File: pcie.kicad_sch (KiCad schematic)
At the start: 10 parts, among them U1 MPFS250T-FCVG484, U17 DSC557-0343FI1

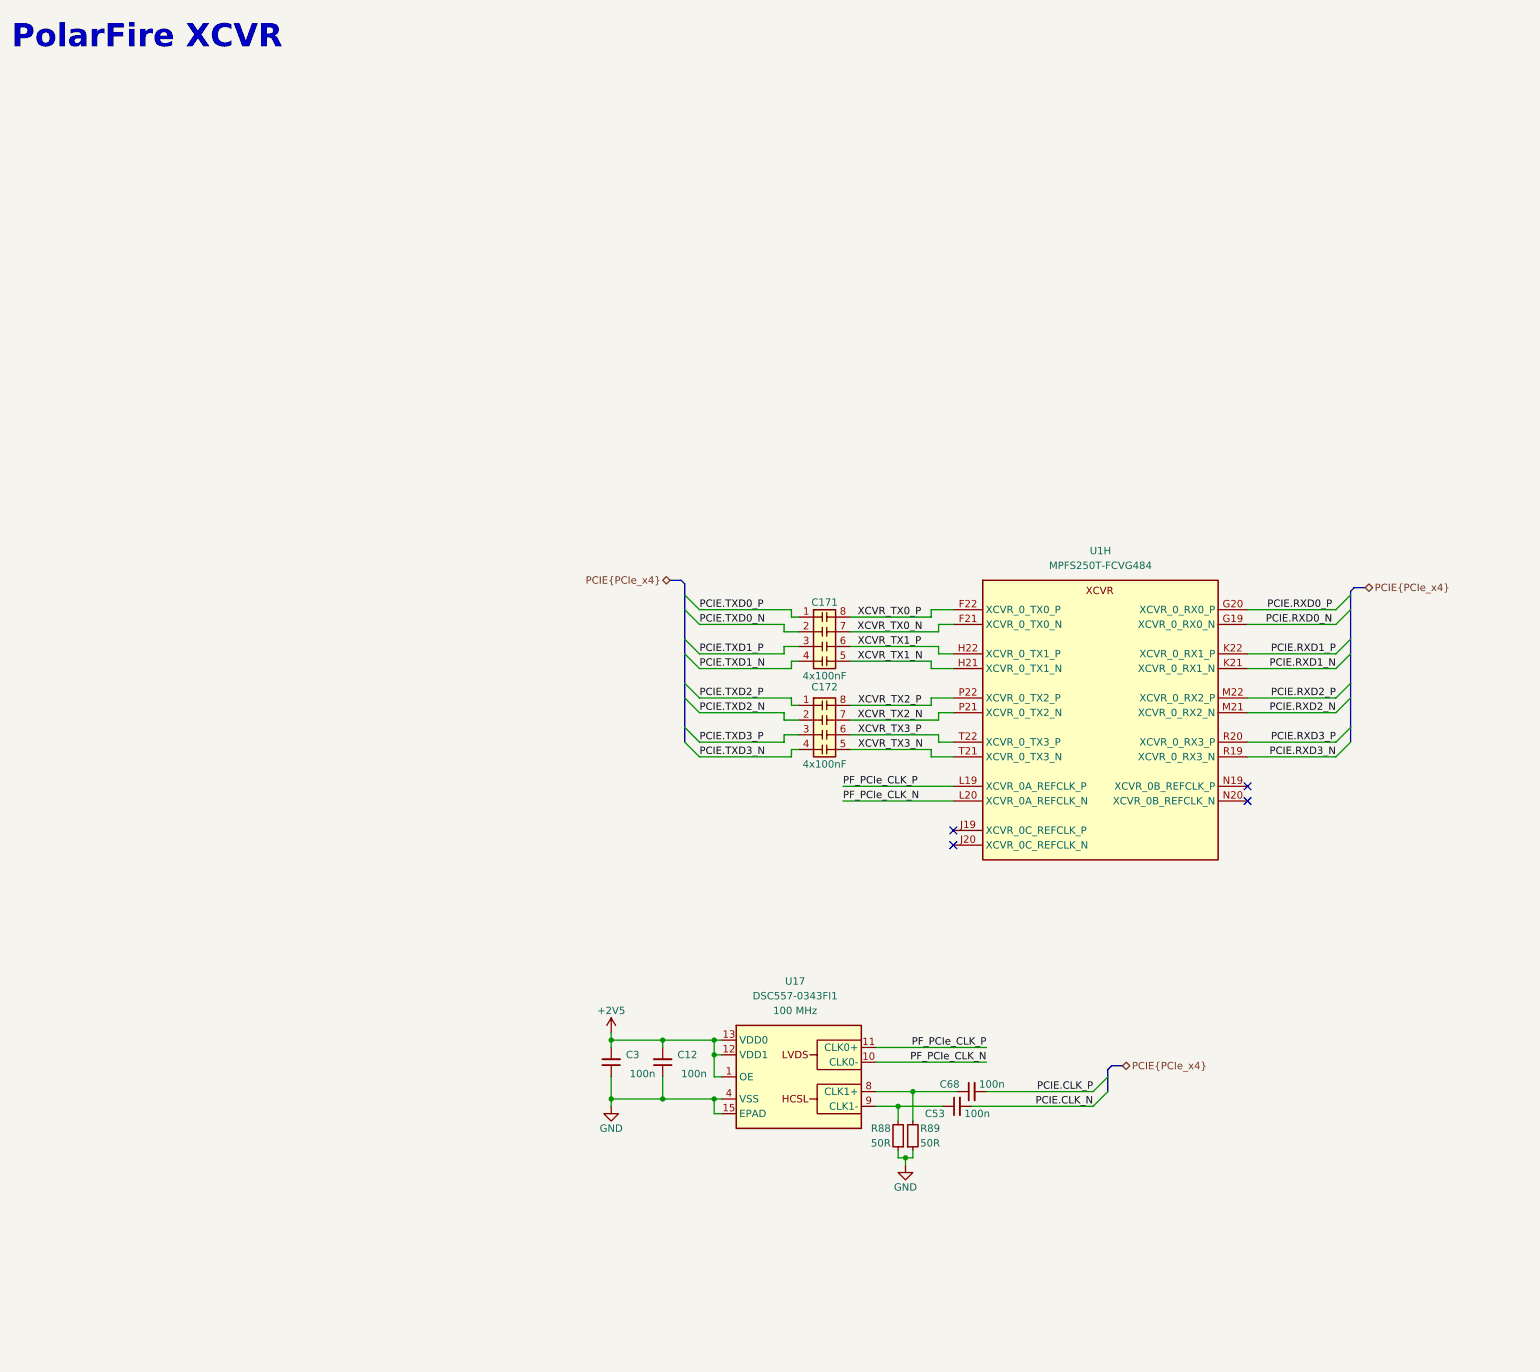
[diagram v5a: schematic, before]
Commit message: [#57422] Align schematics
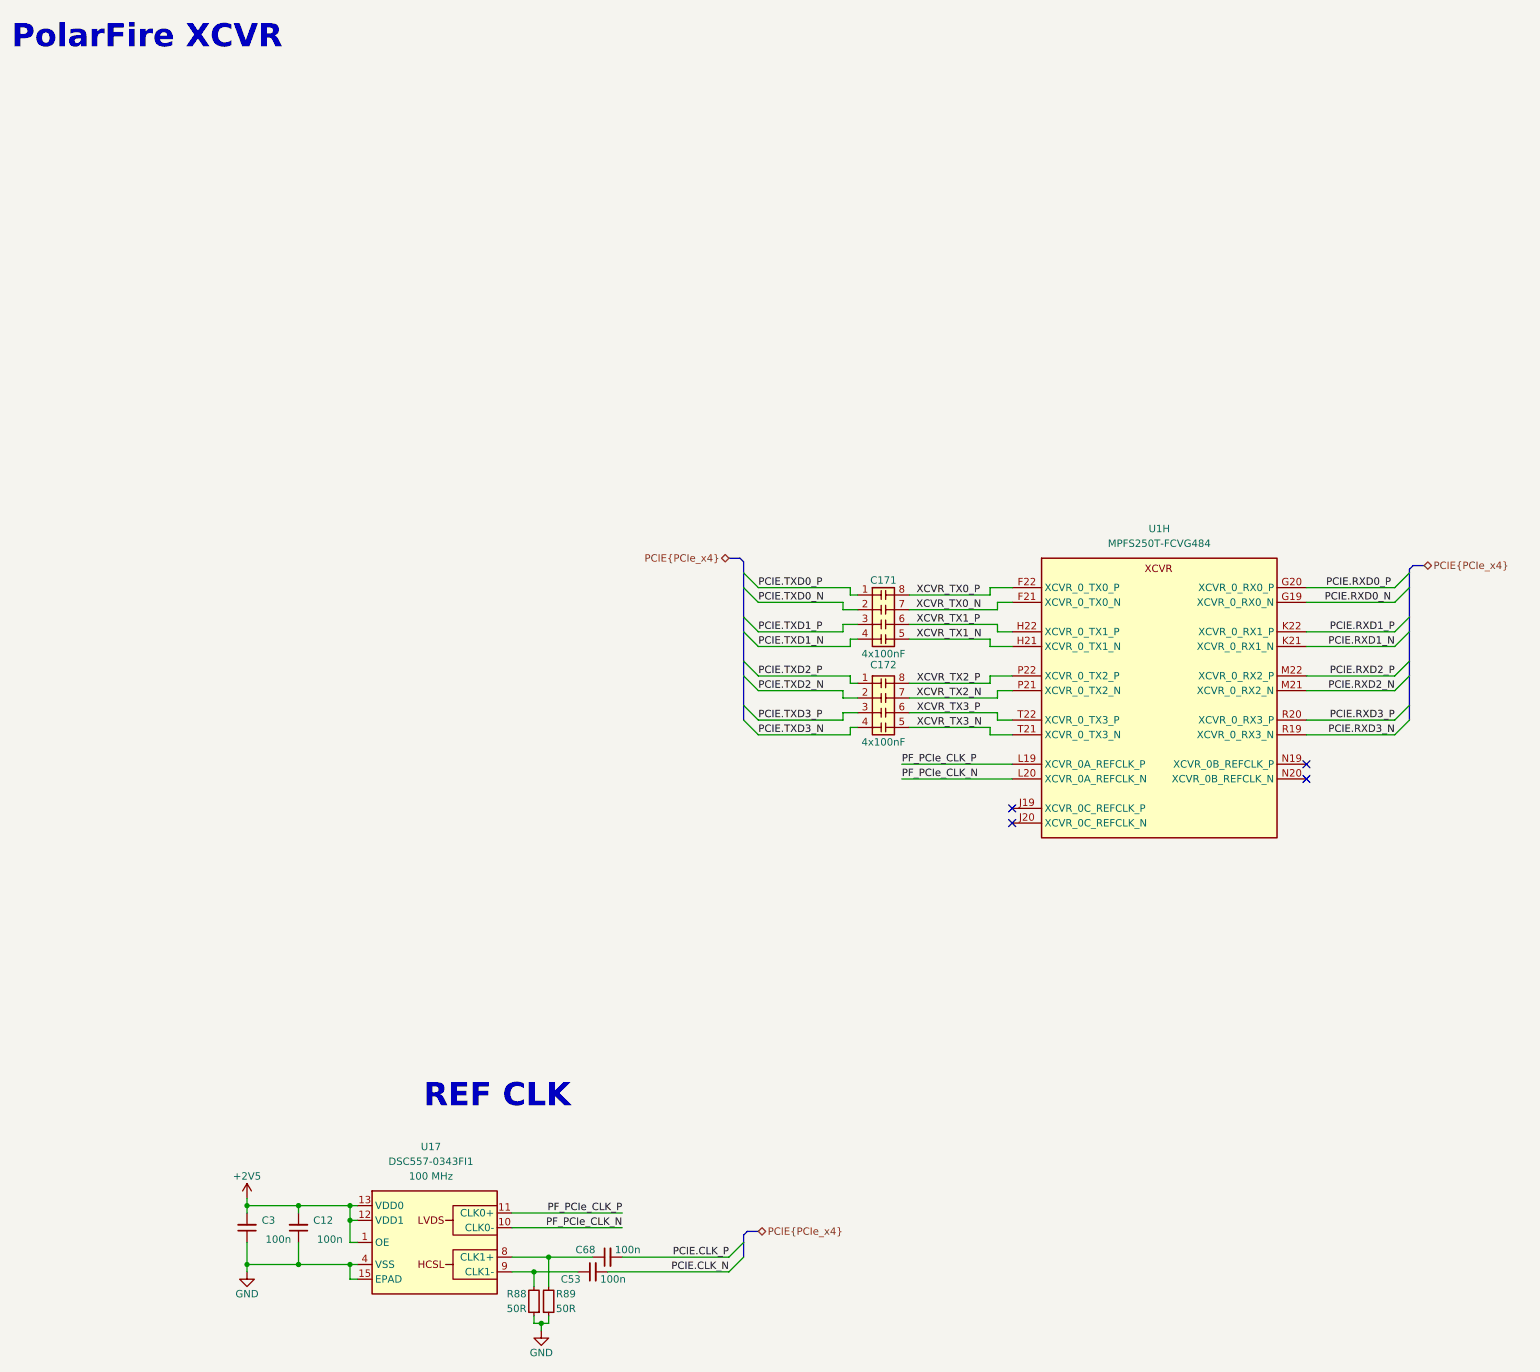
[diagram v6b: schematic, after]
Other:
- note added: "REF CLK"
- moved on the sheet: C12, C171, C172, C3, C53, C68, R88, R89, U17, U1H
